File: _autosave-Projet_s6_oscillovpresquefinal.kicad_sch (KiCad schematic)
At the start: 34 parts, among them IC1 PGA849RGTR, J1 Conn_Coaxial, J2 Conn_01x06_Socket, J3 PILES_3AA, J4 Conn_01x05_Pin, SW1 SW_SPST, U1 MCP6001-OT, U2 AP2112K-3.3, U3 MCP1640x-xCHY, U4 STM32L476RGTx

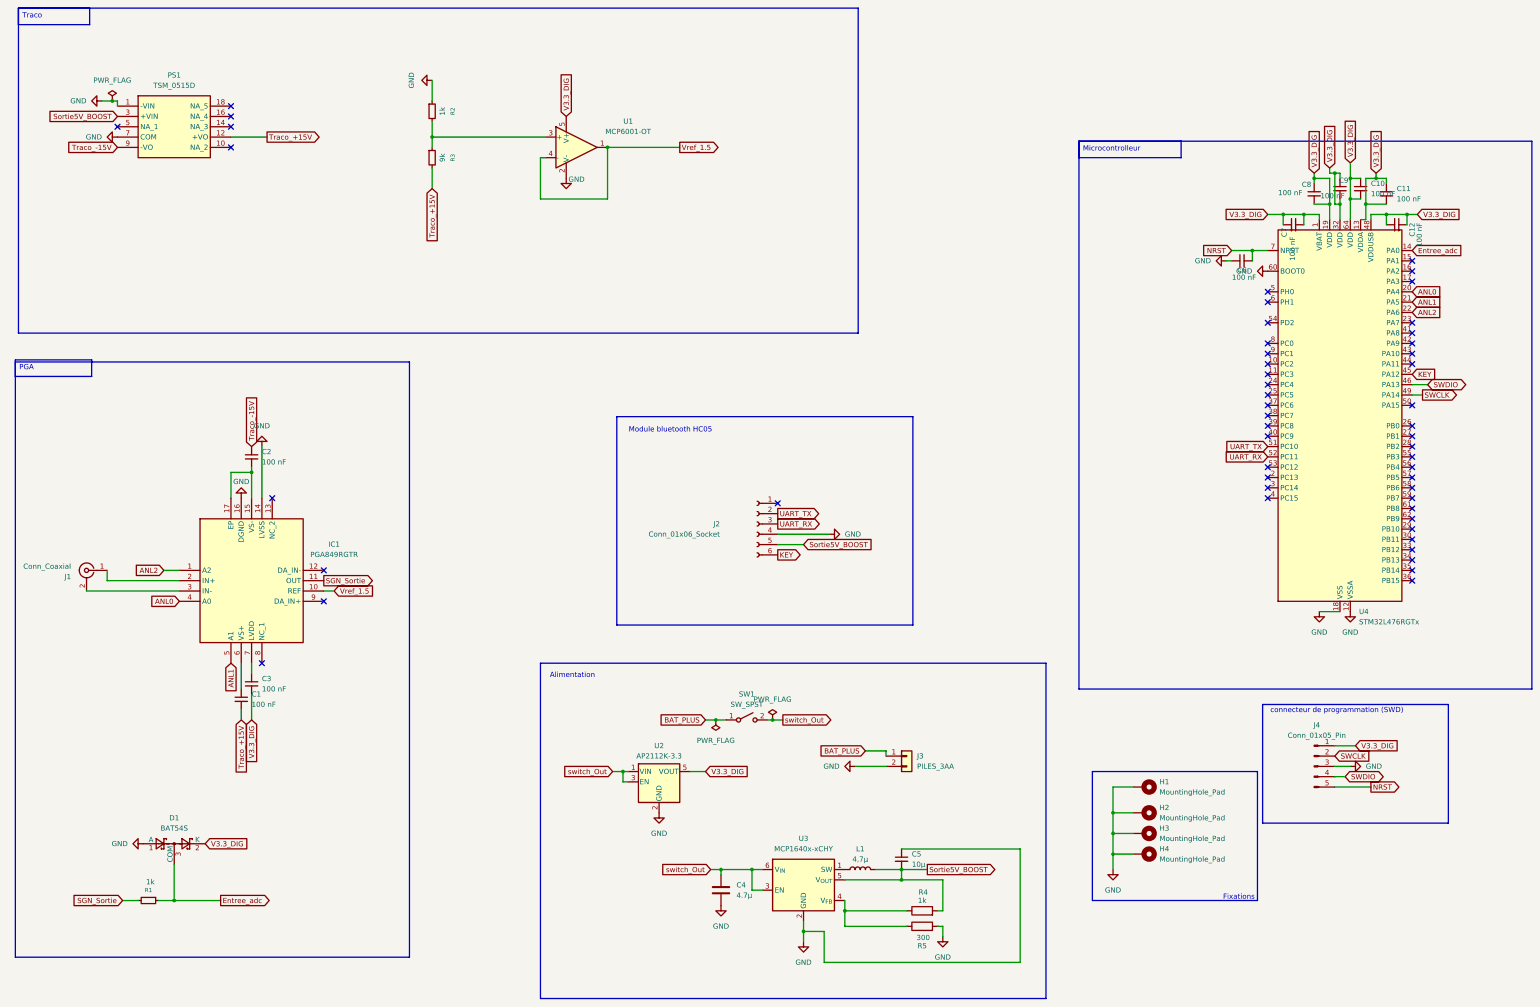
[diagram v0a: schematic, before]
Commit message: Plus d'erreur ERC et empreintes du traco et pga
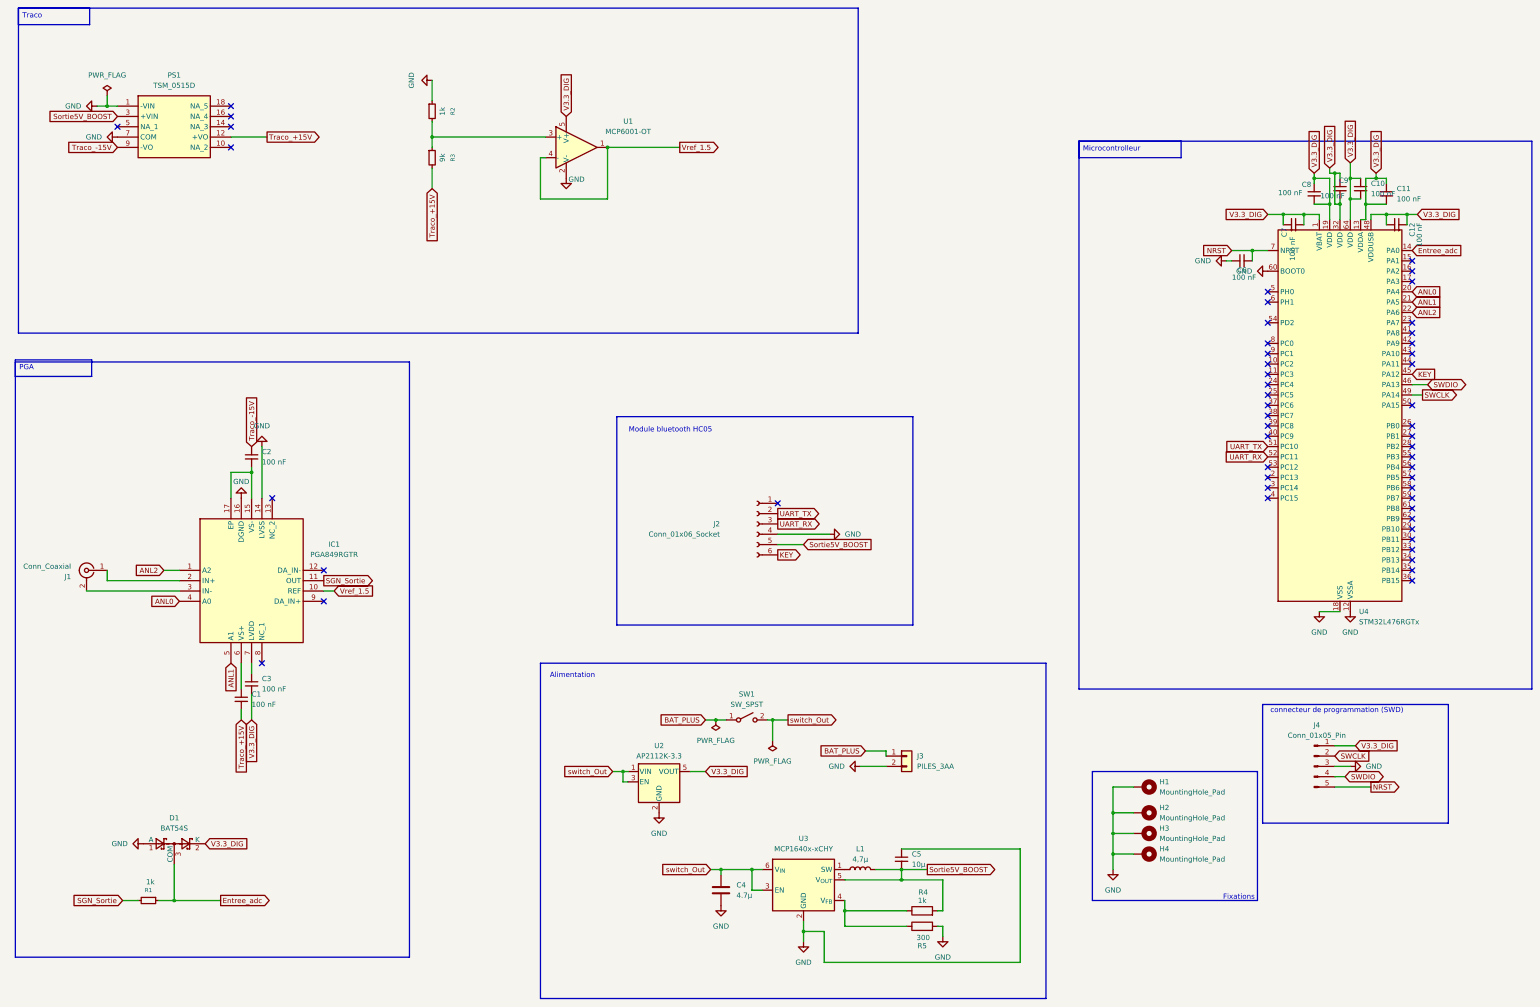
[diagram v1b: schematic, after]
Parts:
- IC1: footprint Empreintes:QFN50P300X300X100-17N-D -> QFN50P300X300X100-17N-D
- PS1: footprint Empreintes:TSM0515D -> TSM0515D
